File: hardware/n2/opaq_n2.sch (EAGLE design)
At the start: 41 parts, among them IC1 RT9013-XXXB, IC2 TS5A3157, IC3 ATSHA204_SOIC8, IC4 ACS712, IC5 ADS1100, IC6 ATMega-328, IC7 AT25F512BWIDE_5.3MM, IC8 LM2594HV, K1 62101021021, X1 16 MHz

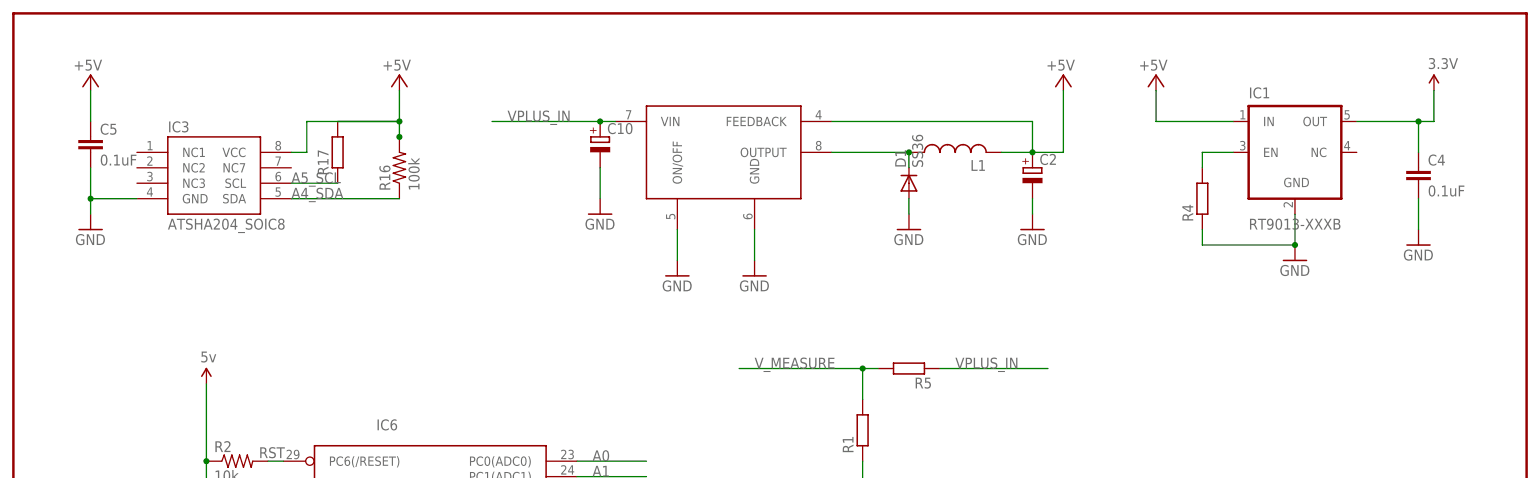
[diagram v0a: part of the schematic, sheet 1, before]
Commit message: Updated the Opaq n1 firmware to read the external temperature and the input voltage. Added the support for the external flash. Renamed the folder of the Opaq n1 hardware.
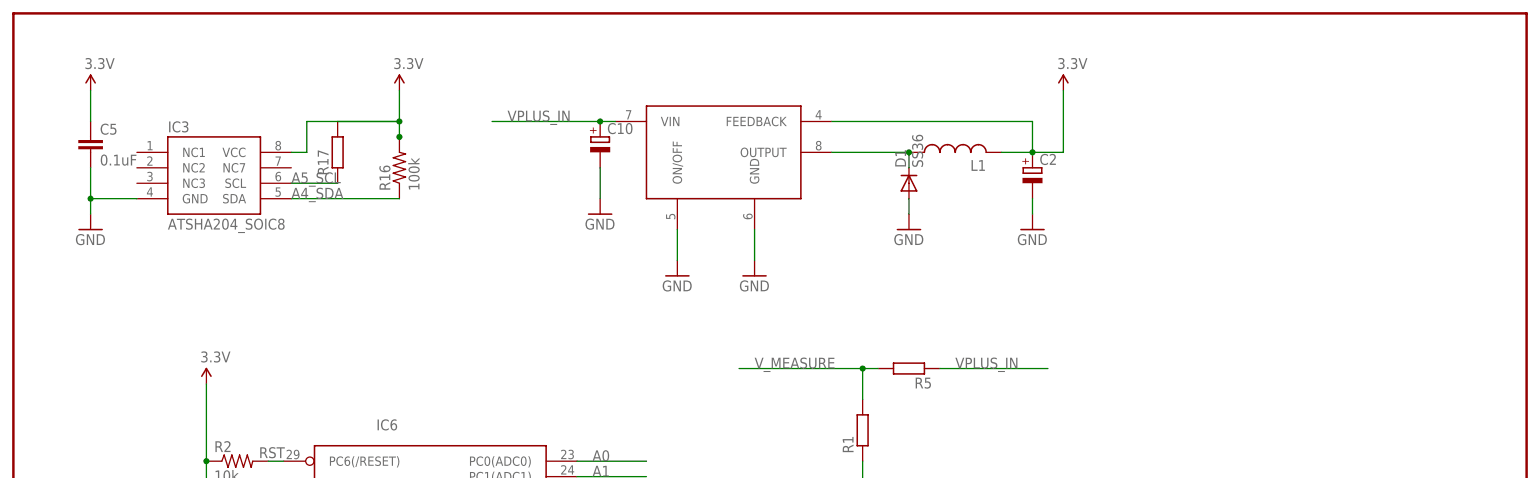
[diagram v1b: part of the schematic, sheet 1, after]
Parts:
- removed C4: 0.1uF, SparkFun-Passives:CAP0805
- removed IC1: RT9013-XXXB, v-reg_extra:RT9013-XXXB
- removed R4: (no value), resistor:R-EU_R0805
- added C8: (no value), resistor:C-EU225-062X268
- added R6: (no value), resistor:R-EU_R2512W
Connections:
- removed net +5V: C2.+, C3.1, C5.1, IC1.IN, IC2.VCC, IC3.VCC, IC4.VCC, IC5.VDD, IC8.FEEDBACK, L1.P$1, R16.2, R17.2
- removed net N$10: IC1.EN, R4.2
- new net L: C8.2, R6.2
- new net LC: C8.1, D2.C, D4.A, R6.1
- new net N: D3.C, D5.A
- new net V+: D4.C, D5.C
- new net V-: D2.A, D3.A
- net 3.3V: now also C2.+, C3.1, C5.1, IC2.VCC, IC3.VCC, IC4.VCC, IC5.VDD, IC6.AVCC, IC6.VCC@1, IC6.VCC@2, IC7.HOLD, IC7.VCC, IC7.WP, IC8.FEEDBACK, L1.P$1, R16.2, R17.2, R2.1; no longer C4.1, IC1.OUT
- net GND: no longer C4.2, IC1.GND, R4.1
- net VCC: no longer IC6.AVCC, IC6.VCC@1, IC6.VCC@2, IC7.HOLD, IC7.VCC, IC7.WP, R2.1
